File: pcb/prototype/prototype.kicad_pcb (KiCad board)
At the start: 2 copper layers, 151.6 x 82.7 mm, 45 parts, among them J1 SDCARD, J2 Bus_ISA_8bit_AB_Rev0, SW1 ADDR SEL, U1 74HC00, U10 74HC74, U11 74HC08, U12 74HC04, U13 74HC74, U2 74HCT32, U3 74HCT139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

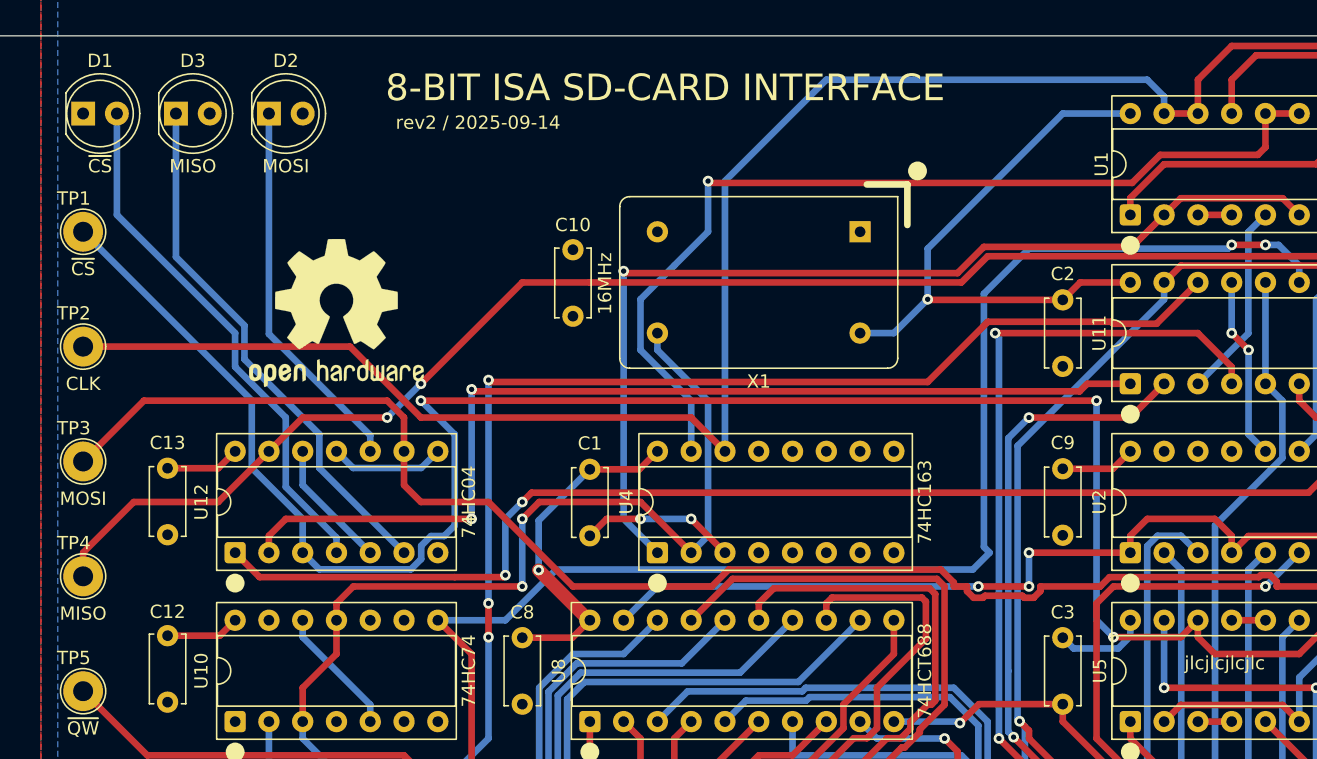
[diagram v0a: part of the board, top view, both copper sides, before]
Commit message: Revising prototype, updating software and adding bracket
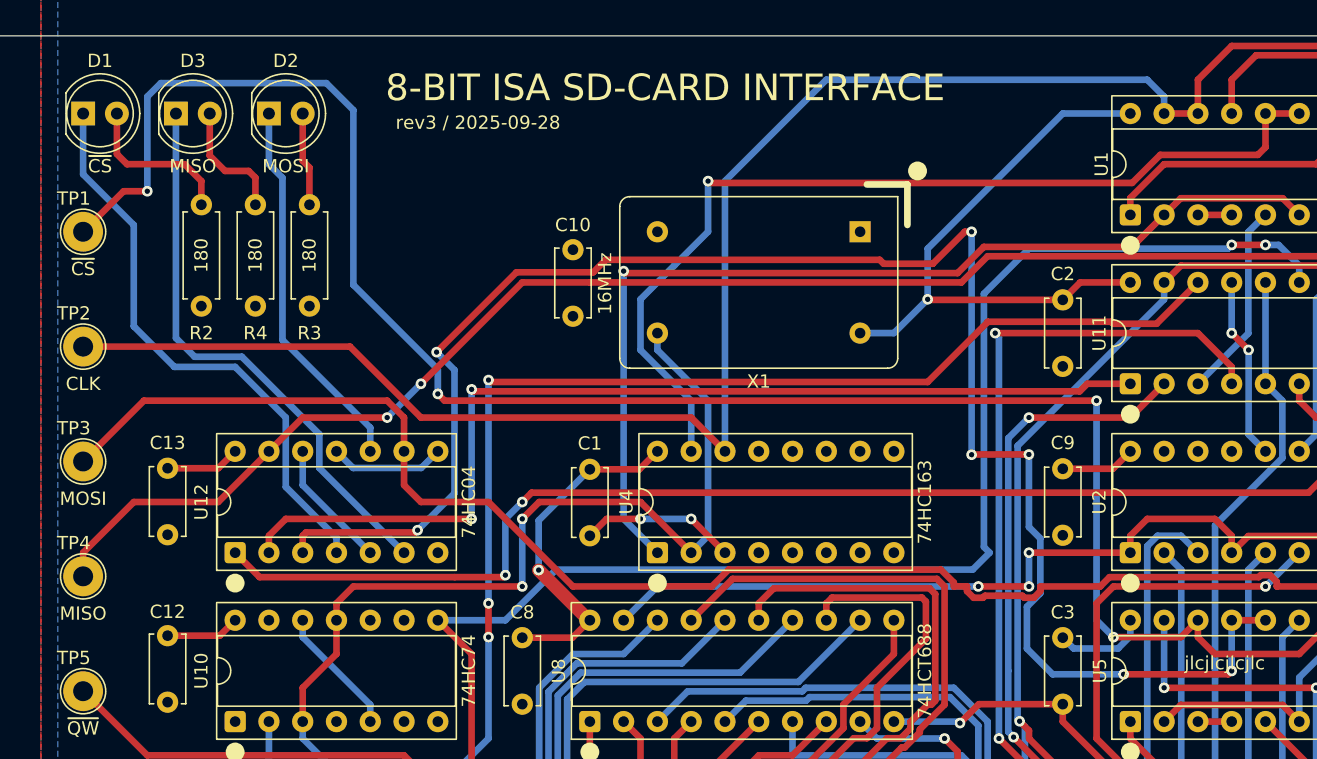
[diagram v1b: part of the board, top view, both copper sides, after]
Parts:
- removed REF**: OSHW-Logo2_14.6x12mm_SilkScreen, Symbol:OSHW-Logo2_14.6x12mm_SilkScreen
- added R2: 180, Resistor_THT:R_Axial_DIN0207_L6.3mm_D2.5mm_P7.62mm_Horizontal, F.Cu at (49.8, 50.3)
- added R3: 180, Resistor_THT:R_Axial_DIN0207_L6.3mm_D2.5mm_P7.62mm_Horizontal, F.Cu at (57.9, 50.3)
- added R4: 180, Resistor_THT:R_Axial_DIN0207_L6.3mm_D2.5mm_P7.62mm_Horizontal, F.Cu at (53.8, 50.3)
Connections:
- D1 pad 1: GND -> Net-(D1-K)
- D2 pad 2: VCC -> Net-(D2-A)
- D3 pad 2: VCC -> Net-(D3-A)
- U12 pad 3: ~{CS} -> CS
- U12 pad 4: Net-(D1-A) -> Net-(D1-K)
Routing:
- net CS: track 2.54 -> 128.5 mm, vias 0 -> 7
- net Net-(D1-K): track 0.00 -> 43.6 mm
- net Net-(D1-A): track 39.9 -> 12.0 mm
- net Net-(D3-A): track 0.00 -> 9.32 mm
- net Net-(D2-A): track 0.00 -> 7.07 mm
- net ~{CS}: track 153.0 -> 150.6 mm, vias 3 -> 4
- net Net-(D3-K): track 40.1 -> 42.2 mm
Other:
- board text added: "rev3 / 2025-09-28"
- board text removed: "rev2 / 2025-09-14"
